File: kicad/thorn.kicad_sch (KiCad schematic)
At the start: 28 parts, among them J1 Conn_01x04, SW1 MX-NoLed-Hotswap, SW10 MX-NoLed-Hotswap, SW11 MX-NoLed-Hotswap, SW12 MX-NoLed-Hotswap, SW13 RotaryEncoder, SW2 MX-NoLed-Hotswap, SW3 MX-NoLed-Hotswap, SW4 MX-NoLed-Hotswap, SW5 MX-NoLed-Hotswap, SW6 MX-NoLed-Hotswap, SW7 MX-NoLed-Hotswap, SW8 MX-NoLed-Hotswap, SW9 MX-NoLed-Hotswap

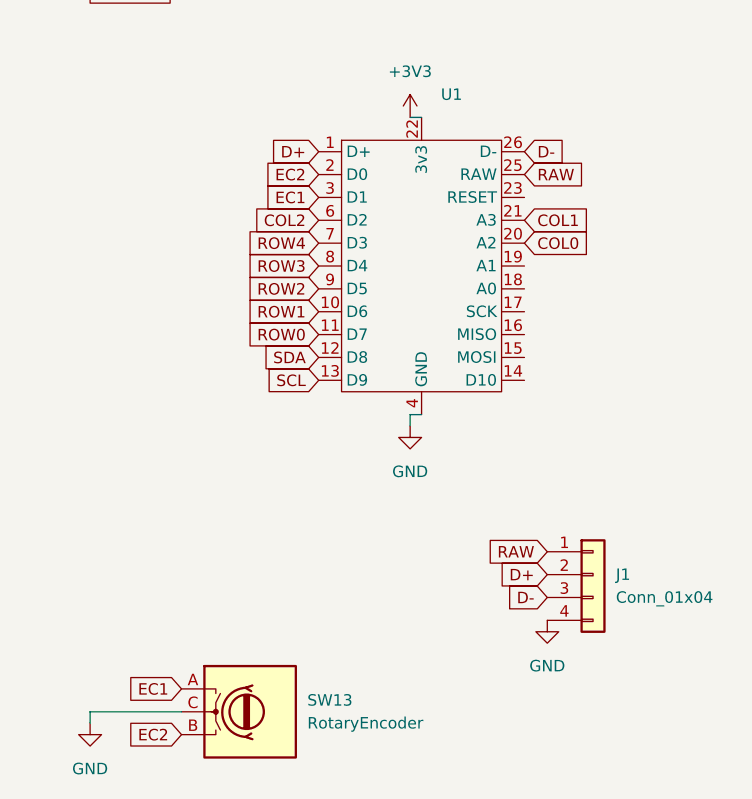
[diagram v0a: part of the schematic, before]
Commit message: fix: changed pinout for data pins on JST connector
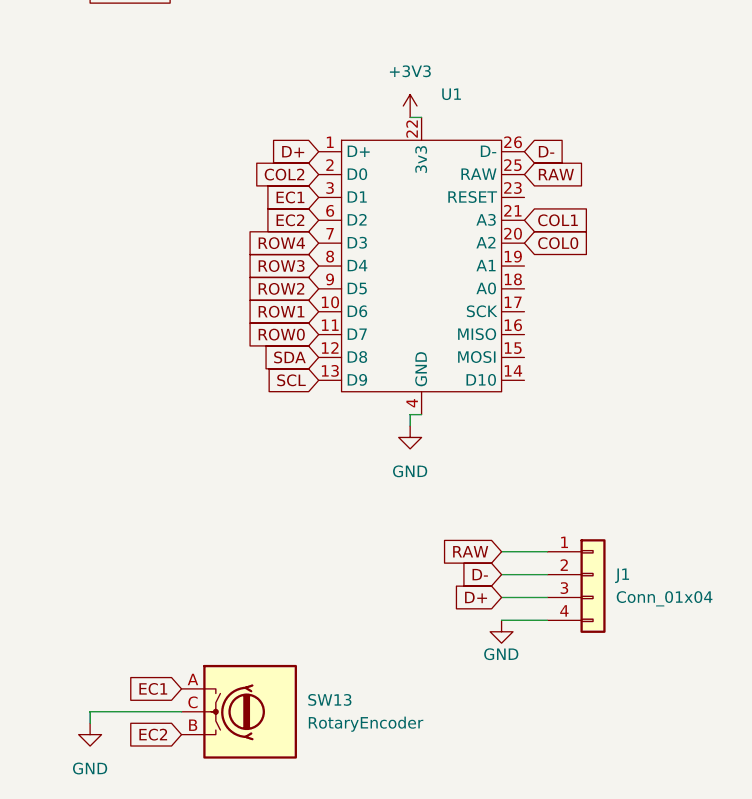
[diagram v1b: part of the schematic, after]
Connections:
- net COL2: now also U1.2 (D0); no longer U1.6 (D2)
- net D+: now also J1.3 (Pin_3); no longer J1.2 (Pin_2)
- net D-: now also J1.2 (Pin_2); no longer J1.3 (Pin_3)
- net EC2: now also U1.6 (D2); no longer U1.2 (D0)

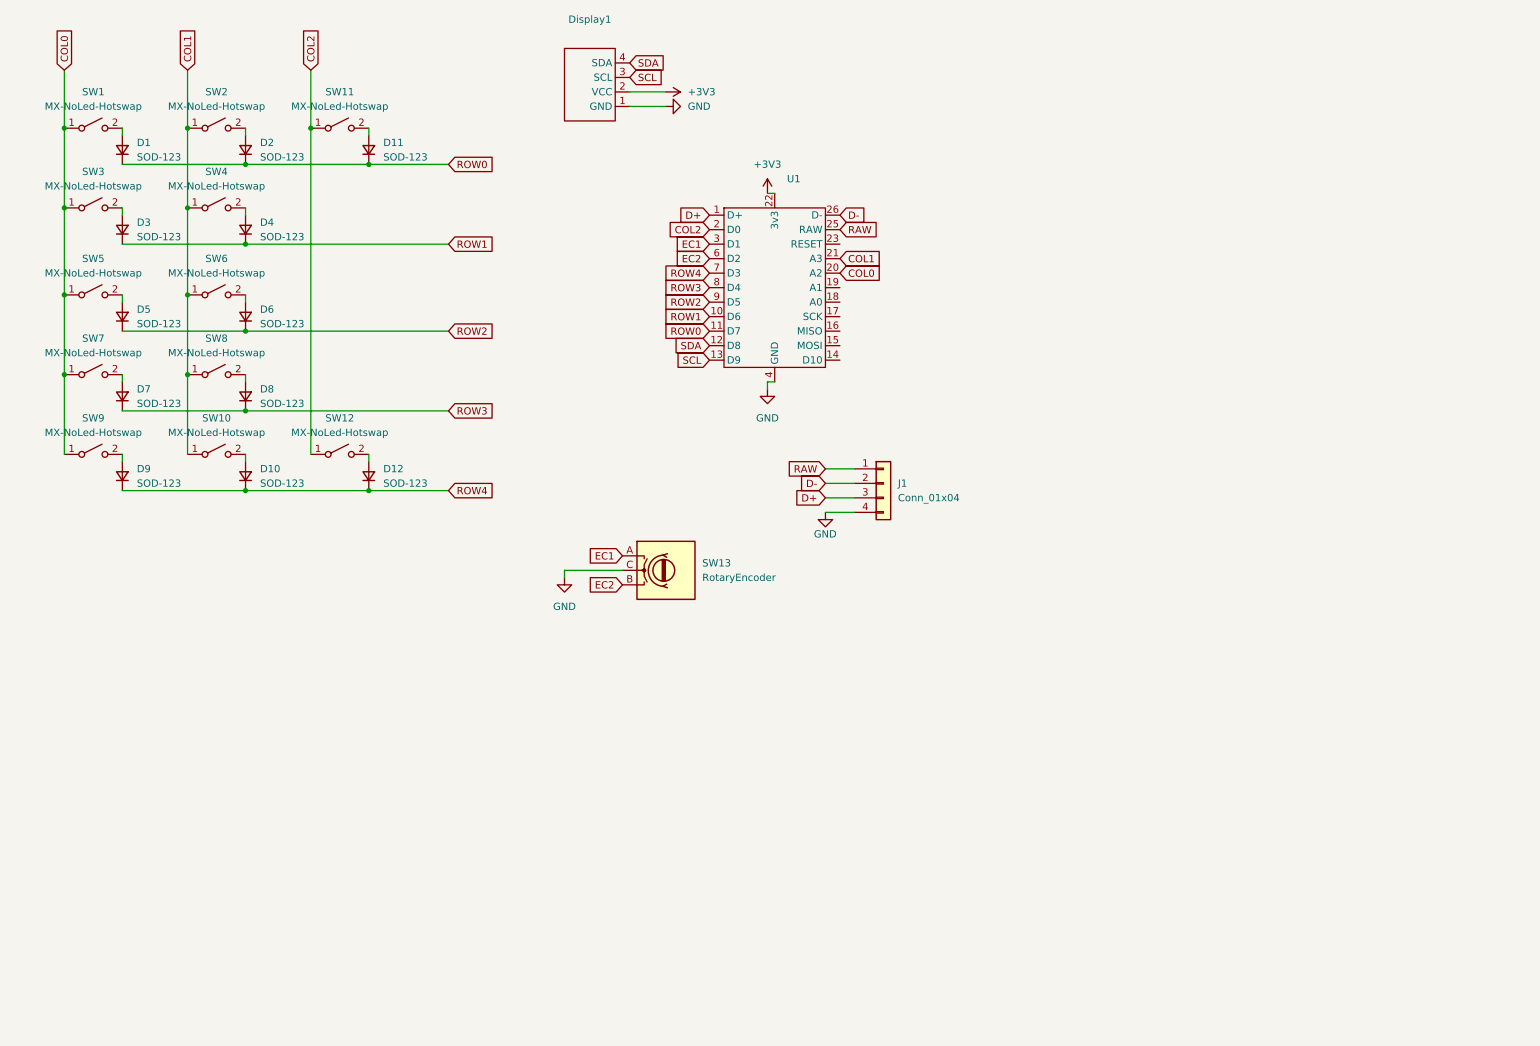
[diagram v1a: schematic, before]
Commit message: feat: change design to implement rp2040
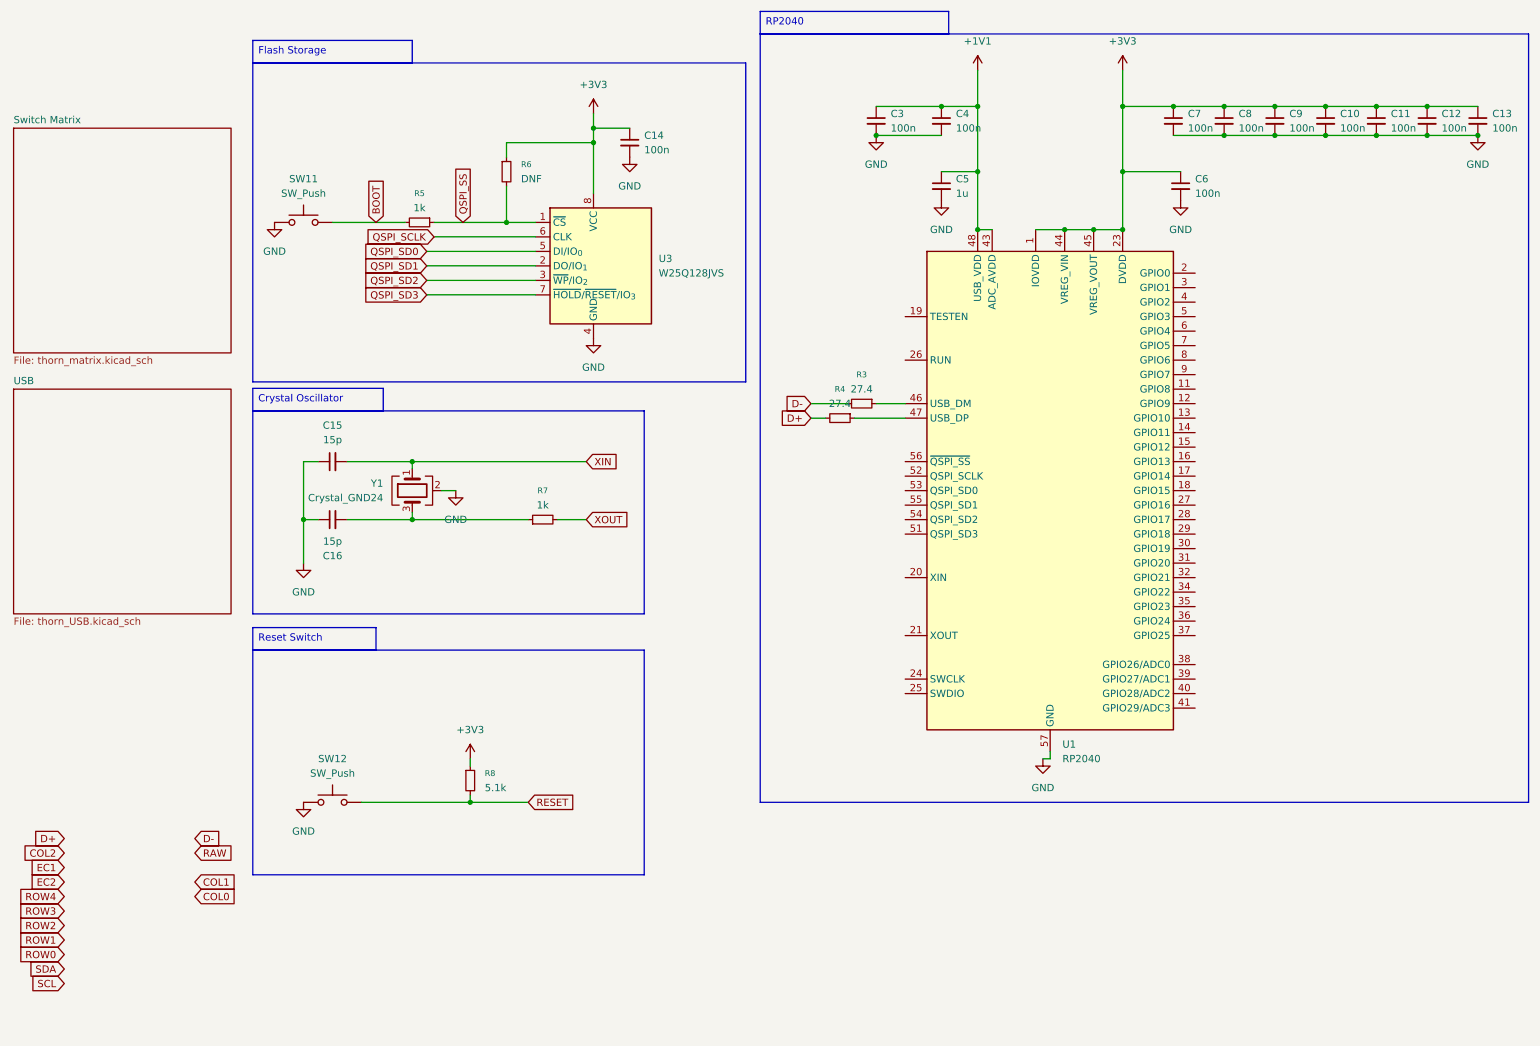
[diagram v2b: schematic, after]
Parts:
- removed D1, D10, D11, D12, D2, D3, D4, D5, D6, D7, D8, D9: SOD-123, Diode_SMD:D_SOD-123, symbol Device:D_Small
- removed Display1: ~, HS91L02W2C01:HS91L02W2C01, symbol HS91L02W2C01:oled_display
- removed J1: Conn_01x04, Connector_JST:JST_SH_SM04B-SRSS-TB_1x04-1MP_P1.00mm_Horizontal, symbol Connector_Generic:Conn_01x04
- removed SW1, SW10, SW11, SW2, SW3, SW4, SW5, SW6, SW7, SW8, SW9: MX-NoLed-Hotswap, MX_Only:MXOnly-1U-Hotswap, symbol Switch:SW_SPST
- removed SW12: MX-NoLed-Hotswap, MX_Only:MXOnly-3U-Hotswap, symbol Switch:SW_SPST
- removed SW13: RotaryEncoder, Rotary_Encoder:RotaryEncoder_Alps_EC12E_Vertical_H20mm, symbol Device:RotaryEncoder
- removed U1: ~, Pro_Micro_Library:KB2040_SMD, symbol Pro_Micro:Pro_Micro
- added C10, C11, C12, C13, C14, C3, C4, C6, C7, C8, C9: 100n, Capacitor_SMD:C_0805_2012Metric, symbol Device:C_Small
- added C15, C16: 15p, Capacitor_SMD:C_0805_2012Metric, symbol Device:C_Small
- added C5: 1u, Capacitor_SMD:C_0805_2012Metric, symbol Device:C_Small
- added R3, R4: 27.4, Resistor_SMD:R_0805_2012Metric, symbol Device:R_Small
- added R5, R7: 1k, Resistor_SMD:R_0805_2012Metric, symbol Device:R_Small
- added R6: DNF, Resistor_SMD:R_0805_2012Metric, symbol Device:R_Small
- added R8: 5.1k, Resistor_SMD:R_0805_2012Metric, symbol Device:R_Small
- added SW11, SW12: SW_Push, Button_Switch_SMD:SW_Push_1P1T_XKB_TS-1187A, symbol Switch:SW_Push
- added U1: RP2040, Package_DFN_QFN:QFN-56-1EP_7x7mm_P0.4mm_EP3.2x3.2mm, symbol MCU_RaspberryPi:RP2040
- added U3: W25Q128JVS, Package_SO:SOIC-8_5.3x5.3mm_P1.27mm, symbol Memory_Flash:W25Q128JVS
- added Y1: Crystal_GND24, Crystal:Crystal_SMD_3225-4Pin_3.2x2.5mm, symbol Device:Crystal_GND24
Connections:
- net +3V3: now also C10.1, C11.1, C12.1, C13.1, C14.1, C6.1, C7.1, C8.1, C9.1, R6.1, R8.1, U1.1 (IOVDD), U1.10 (IOVDD), U1.22 (IOVDD), U1.23 (DVDD), U1.33 (IOVDD), U1.42 (IOVDD), U1.44 (VREG_VIN), U1.45 (VREG_VOUT), U1.49 (IOVDD), U1.50 (DVDD), U3.8 (VCC)
- net D+: now also R4.2
- net D-: now also R3.2
- net GND: now also C10.2, C11.2, C12.2, C13.2, C14.2, C15.1, C16.1, C3.2, C4.2, C5.2, C6.2, C7.2, C8.2, C9.2, SW11.1, SW12.1, U1.57 (GND), U3.4 (GND), Y1.2 (G), Y1.4 (G)
- new net: C16.2, R7.1, Y1.3
- new net: R4.1, U1.47 (USB_DP)
- new net: R3.1, U1.46 (USB_DM)
- new net +1V1: C3.1, C4.1, C5.1, U1.43 (ADC_AVDD), U1.48 (USB_VDD)
- new net BOOT: R5.2, SW11.2
- new net QSPI_SCLK: U3.6 (CLK)
- new net QSPI_SD0: U3.5 (DI/IO_{0})
- new net QSPI_SD1: U3.2 (DO/IO_{1})
- new net QSPI_SD2: U3.3 (~{WP}/IO_{2})
- new net QSPI_SD3: U3.7 (~{HOLD}/~{RESET}/IO_{3})
- new net QSPI_SS: R5.1, R6.2, U3.1 (~{CS})
- new net RESET: R8.2, SW12.2
- new net XIN: C15.2, Y1.1
- new net XOUT: R7.2
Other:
- added sheet Switch Matrix (thorn_matrix.kicad_sch)
- added sheet USB (thorn_USB.kicad_sch)

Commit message: chore: cleaned up schematic
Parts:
- added J3: Conn_01x09, symbol Connector_Generic:Conn_01x09
- C6: value 100n -> 1u
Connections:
- net COL0: now also U1.37 (GPIO25)
- net COL1: now also U1.36 (GPIO24)
- net GND: now also U1.19 (TESTEN)
- net QSPI_SCLK: now also U1.52 (QSPI_SCLK)
- net QSPI_SD0: now also U1.53 (QSPI_SD0)
- net QSPI_SD1: now also U1.55 (QSPI_SD1)
- net QSPI_SD2: now also U1.54 (QSPI_SD2)
- net QSPI_SD3: now also U1.51 (QSPI_SD3)
- net QSPI_SS: now also U1.56 (~{QSPI_SS})
- net RESET: now also U1.26 (RUN)
- net ROW0: now also U1.30 (GPIO19)
- net ROW1: now also U1.31 (GPIO20)
- net ROW2: now also U1.32 (GPIO21)
- net ROW3: now also U1.34 (GPIO22)
- net ROW4: now also U1.35 (GPIO23)
- net XIN: now also U1.20 (XIN)
- net XOUT: now also U1.21 (XOUT)
- net SWCLK: now reaches U1.24 (SWCLK)
- net SWDIO: now reaches U1.25 (SWDIO)

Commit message: feat: finished preliminary wiring
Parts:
- removed J3: Conn_01x09, symbol Connector_Generic:Conn_01x09
- added J5, J7: Conn_01x07, Connector_FFC-FPC:Molex_200528-0070_1x07-1MP_P1.00mm_Horizontal, symbol Connector_Generic:Conn_01x07
- added U4: SRV05-4, Package_TO_SOT_SMD:SOT-23-6, symbol Power_Protection:SRV05-4
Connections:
- net +3V3: now also J7.2 (Pin_2)
- net COL0: now also U1.2 (GPIO0), J5.1 (Pin_1); no longer U1.37 (GPIO25)
- net COL1: now also U1.3 (GPIO1), J5.2 (Pin_2); no longer U1.36 (GPIO24)
- net D+: now also U4.1 (IO1)
- net D-: now also U4.6 (IO4)
- net GND: now also J7.4 (Pin_4), J7.6 (Pin_6), U4.2 (VN)
- net ROW0: now also U1.8 (GPIO6), J5.7 (Pin_7); no longer U1.30 (GPIO19)
- net ROW1: now also U1.7 (GPIO5), J5.6 (Pin_6); no longer U1.31 (GPIO20)
- net ROW2: now also U1.6 (GPIO4), J5.5 (Pin_5); no longer U1.32 (GPIO21)
- net ROW3: now also U1.5 (GPIO3), J5.4 (Pin_4); no longer U1.34 (GPIO22)
- net ROW4: now also U1.4 (GPIO2), J5.3 (Pin_3); no longer U1.35 (GPIO23)
- net SCL: now also U1.9 (GPIO7), J7.1 (Pin_1)
- net SDA: now also U1.11 (GPIO8), J7.3 (Pin_3)
- net EC1: now reaches U1.12 (GPIO9)
- net EC1: now also J7.5 (Pin_5)
- net EC2: now reaches U1.13 (GPIO10)
- net EC2: now also J7.7 (Pin_7)
- new net +5V: U4.5 (VP)
- no-connect marks 0 -> 2
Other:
- moved on the sheet: C10, C11, C12, C13, C14, C15, C16, C3, C4, C5, C6, C7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

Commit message: feat: change pcb to preliminary final design
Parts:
- removed U4: SRV05-4, Package_TO_SOT_SMD:SOT-23-6, symbol Power_Protection:SRV05-4
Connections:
- no-connect marks 2 -> 0
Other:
- moved on the sheet: J5, J7
